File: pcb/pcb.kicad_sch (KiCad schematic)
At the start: 24 parts, among them J1 USB_C_Receptacle_USB2.0_16P, SW1 SW_Push, U1 USBLC6-2SC6, U2 XC6206PxxxMR, U3 STM32F072CBTx

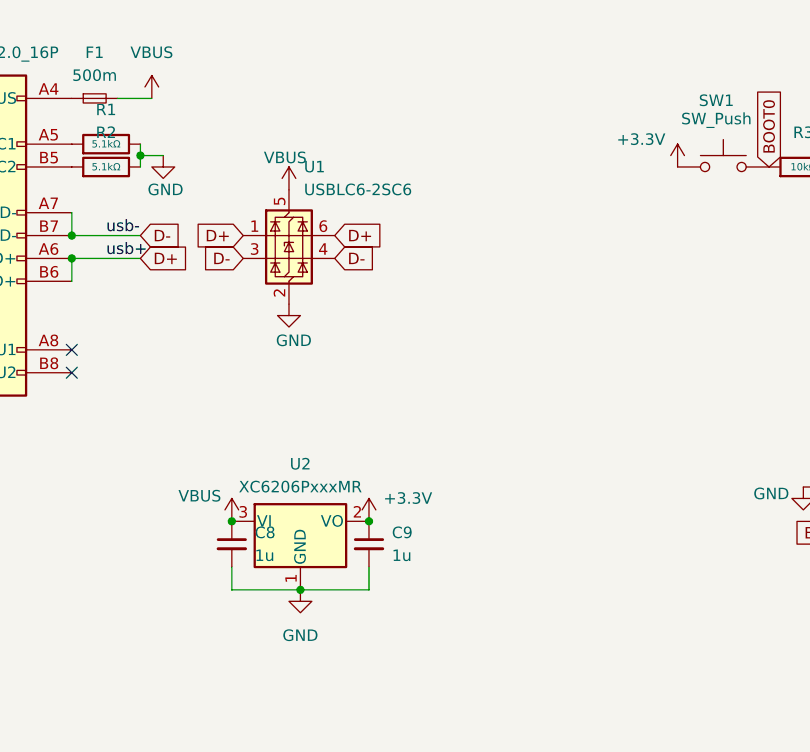
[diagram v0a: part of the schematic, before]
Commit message: Replace some more with LSCPCB library
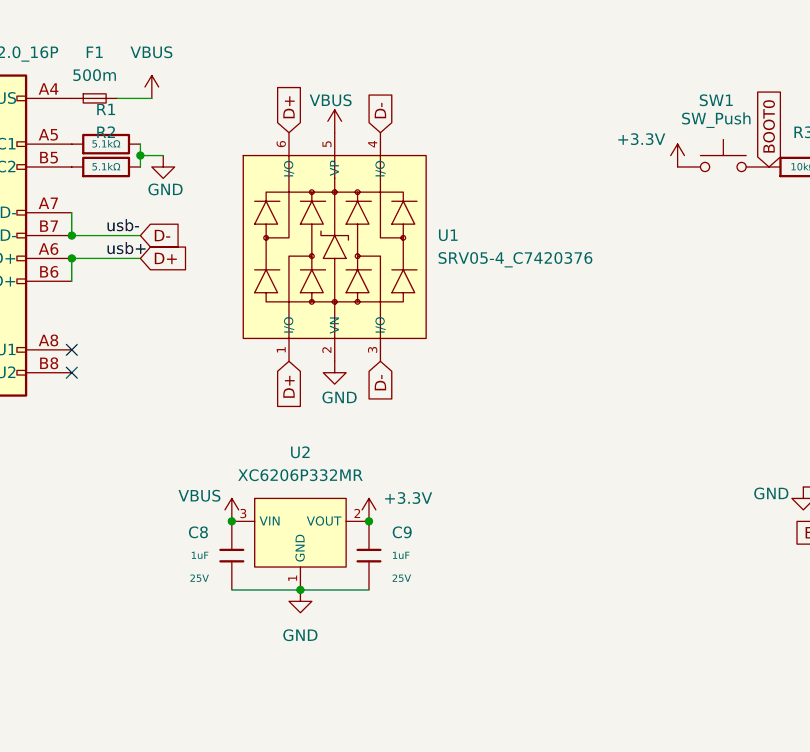
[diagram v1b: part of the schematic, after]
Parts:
- removed C8, C9: 1u, Capacitor_SMD:C_0402_1005Metric, symbol Device:C_Small
- removed U1: USBLC6-2SC6, PCM_marbastlib-various:SOT-23-6-routable, symbol Power_Protection:USBLC6-2SC6
- removed U2: XC6206PxxxMR, Package_TO_SOT_SMD:SOT-23-3, symbol Regulator_Linear:XC6206PxxxMR
- added C8, C9: 1uF, PCM_JLCPCB:C_0402, symbol PCM_JLCPCB-Capacitors:0402,1uF
- added U1: SRV05-4_C7420376, PCM_JLCPCB:SOT-23-6_L2.9-W1.6-P0.95-LS2.8-BL-1, symbol PCM_JLCPCB-Diode-Packages:Package, SRV05-4_C7420376
- added U2: XC6206P332MR, PCM_JLCPCB:SOT-23-3_L2.9-W1.6-P1.90-LS2.8-BR, symbol PCM_JLCPCB-Power:LDO, 3.3V, 0.2A
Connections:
- net +3.3V: now also C9.1, U2.2 (VOUT)
- net D+: now also U1.1 (I/O), U1.6 (I/O)
- net D-: now also U1.3 (I/O), U1.4 (I/O)
- net GND: now also C8.2, C9.2, U1.2 (VN), U2.1 (GND)
- net VBUS: now also C8.1, U1.5 (VP), U2.3 (VIN)

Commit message: matrix connected
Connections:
- net Co10: now also U3.17 (PA7); no longer U3.3 (PC14)
- net Co11: now also U3.16 (PA6); no longer U3.17 (PA7)
- net Co12: now also U3.15 (PA5); no longer U3.10 (PA0)
- net Co13: now also U3.14 (PA4); no longer U3.11 (PA1)
- net Co14: now also U3.13 (PA3); no longer U3.12 (PA2)
- net Co15: now also U3.12 (PA2); no longer U3.13 (PA3)
- net Co5: now also U3.22 (PB11); no longer U3.14 (PA4)
- net Co7: now also U3.20 (PB2); no longer U3.22 (PB11)
- net Co8: now also U3.19 (PB1); no longer U3.15 (PA5)
- net Co9: now also U3.18 (PB0); no longer U3.2 (PC13)
- net Ro2: now also U3.11 (PA1); no longer U3.4 (PC15)
- net Ro3: now also U3.10 (PA0); no longer U3.18 (PB0)
- net Ro4: now also U3.4 (PC15); no longer U3.19 (PB1)
- net Ro5: now also U3.3 (PC14); no longer U3.20 (PB2)
- net Ro6: now also U3.2 (PC13); no longer U3.16 (PA6)
- no-connect marks 2 -> 12

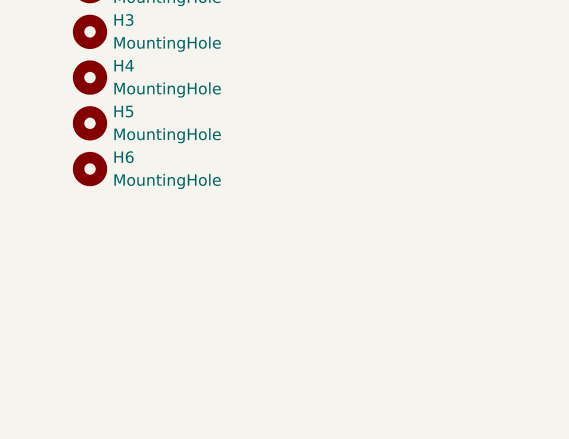
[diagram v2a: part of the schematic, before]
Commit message: fix mouting holes
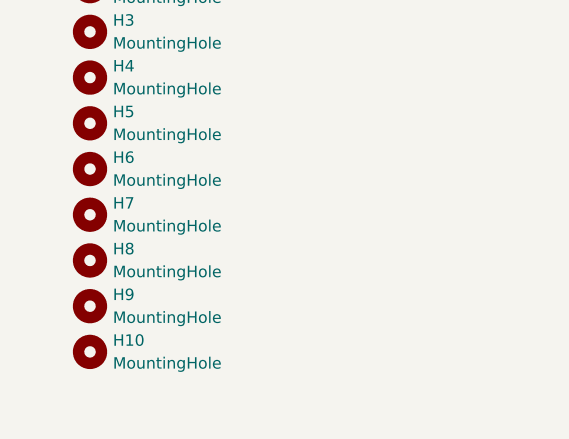
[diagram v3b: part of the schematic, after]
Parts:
- added H10, H7, H8, H9: MountingHole, MountingHole:MountingHole_2mm, symbol Mechanical:MountingHole

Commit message: jlcpcb USB-C
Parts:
- removed J1: USB_C_Receptacle_USB2.0_16P, PCM_marbastlib-various:USB_C_Receptacle_HRO_TYPE-C-31-M-12, symbol Connector:USB_C_Receptacle_USB2.0_16P
- added J1: Connector, USB-TYPE-C-16P, PCM_JLCPCB:TYPE-C-SMD_HX-TYPE-C-16PIN, symbol PCM_JLCPCB-Extended:Connector, USB-TYPE-C-16P
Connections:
- net D+: now also J1.A6 (D+), J1.B6 (D+)
- net D-: now also J1.A7 (D-), J1.B7 (D-)
- net GND: now also J1.A12B1 (GND), J1.B12A1 (GND), J1.S1 (SHIELD)
- net at R1.1: now also J1.A5 (CC1)
- net at R2.1: now also J1.B5 (CC2)
- net at F1.1: now also J1.A9B4 (VBUS), J1.B9A4 (VBUS)
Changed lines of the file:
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@@
 	)
 	(junction
+		(at 57.15 40.64)
+		(diameter 0)
+		(color 0 0 0 0)
+	)
+	(junction
 		(at 232.41 55.88)
 		(diameter 0)
@@
 	)
 	(junction
-		(at 57.15 40.64)
-		(diameter 0)
-		(color 0 0 0 0)
-	)
-	(junction
 		(at 57.15 43.18)
 		(diameter 0)
@@
 		(dnp no)
 		(fields_autoplaced yes)
-		(property "Reference" "#PWR04"
+		(property "Reference" "#PWR05"
 			(at 142.24 39.37 0)
 			(effects
@@
 			(project ""
 				(path "/c1d39311-56a5-4035-b0a7-7ad71eed89a6"
-					(reference "#PWR04")
+					(reference "#PWR05")
 					(unit 1)
 				)
@@
 		(on_board yes)
 		(dnp no)
-		(property "Reference" "#PWR06"
+		(property "Reference" "#PWR07"
 			(at 86.36 60.96 0)
 			(effects
@@
 			(project ""
 				(path "/c1d39311-56a5-4035-b0a7-7ad71eed89a6"
-					(reference "#PWR06")
+					(reference "#PWR07")
 					(unit 1)
 				)
@@
 		(dnp no)
 		(fields_autoplaced yes)
-		(property "Reference" "#PWR07"
+		(property "Reference" "#PWR06"
 			(at 196.85 52.07 0)
 			(effects
@@
 			(project ""
 				(path "/c1d39311-56a5-4035-b0a7-7ad71eed89a6"
-					(reference "#PWR07")
+					(reference "#PWR06")
 					(unit 1)
 				)
@@
 		(on_board yes)
 		(dnp no)
-		(property "Reference" "#PWR05"
+		(property "Reference" "#PWR02"
 			(at 86.36 33.02 0)
 			(effects
@@
 			(project ""
 				(path "/c1d39311-56a5-4035-b0a7-7ad71eed89a6"
-					(reference "#PWR05")
+					(reference "#PWR02")
 					(unit 1)
 				)
@@
 		(on_board yes)
 		(dnp no)
-		(property "Reference" "#PWR03"
+		(property "Reference" "#PWR04"
 			(at 124.46 36.83 0)
 			(effects
@@
 			(project ""
 				(path "/c1d39311-56a5-4035-b0a7-7ad71eed89a6"
-					(reference "#PWR03")
+					(reference "#PWR04")
 					(unit 1)
 				)
@@
 		(on_board yes)
 		(dnp no)
-		(property "Reference" "#PWR02"
+		(property "Reference" "#PWR03"
 			(at 67.31 38.1 0)
 			(effects
@@
 			(project ""
 				(path "/c1d39311-56a5-4035-b0a7-7ad71eed89a6"
-					(reference "#PWR02")
+					(reference "#PWR03")
 					(unit 1)
 				)
@@
 	)
 	(symbol
-		(lib_id "Connector:USB_C_Receptacle_USB2.0_16P")
-		(at 41.91 40.64 0)
-		(unit 1)
-		(exclude_from_sim no)
-		(in_bom yes)
-		(on_board yes)
-		(dnp no)
-		(fields_autoplaced yes)
-		(property "Reference" "J1"
-			(at 41.91 17.78 0)
-			(effects
-				(font
-					(size 1.27 1.27)
-				)
-			)
-		)
-		(property "Value" "USB_C_Receptacle_USB2.0_16P"
-			(at 41.91 20.32 0)
-			(effects
-				(font
-					(size 1.27 1.27)
-				)
-			)
-		)
-		(property "Footprint" "PCM_marbastlib-various:USB_C_Receptacle_HRO_TYPE-C-31-M-12"
-			(at 45.72 40.64 0)
-			(effects
-				(font
-					(size 1.27 1.27)
-				)
-				(hide yes)
-			)
-		)
-		(property "Datasheet" "https://www.usb.org/sites/default/files/documents/usb_type-c.zip"
-			(at 45.72 40.64 0)
-			(effects
-				(font
-					(size 1.27 1.27)
-				)
-				(hide yes)
-			)
-		)
-		(property "Description" "USB 2.0-only 16P Type-C Receptacle connector"
-			(at 41.91 40.64 0)
-			(effects
-				(font
-					(size 1.27 1.27)
-				)
-				(hide yes)
-			)
-		)
-		(pin "A6"
-		)
-		(pin "B7"
-		)
-		(pin "B4"
-		)
-		(pin "B6"
-		)
-		(pin "A5"
-		)
-		(pin "B9"
-		)
-		(pin "A7"
-		)
-		(pin "S1"
-		)
-		(pin "A9"
-		)
-		(pin "B12"
-		)
-		(pin "B1"
-		)
-		(pin "A12"
-		)
-		(pin "A1"
-		)
-		(pin "A4"
-		)
-		(pin "A8"
-		)
-		(pin "B5"
-		)
-		(pin "B8"
-		)
-		(instances
-			(project ""
-				(path "/c1d39311-56a5-4035-b0a7-7ad71eed89a6"
-					(reference "J1")
-					(unit 1)
-				)
-			)
-		)
-	)
-	(symbol
 		(lib_id "PCM_JLCPCB-Capacitors:0402,10uF")
 		(at 241.3 52.07 0)
@@
 					(unit 1)
 				)
+			)
+		)
+	)
+	(symbol
+		(lib_id "PCM_JLCPCB-Extended:Connector, USB-TYPE-C-16P")
+		(at 41.91 40.64 0)
+		(unit 1)
+		(exclude_from_sim no)
+		(in_bom yes)
+		(on_board yes)
+		(dnp no)
+		(fields_autoplaced yes)
+		(property "Reference" "J1"
+			(at 41.91 20.32 0)
+			(effects
+				(font
+					(size 1.27 1.27)
+				)
+			)
+		)
+		(property "Value" "Connector, USB-TYPE-C-16P"
+			(at 44.45 41.91 0)
+			(effects
+				(font
+					(size 1.27 1.27)
+				)
+				(hide yes)
+			)
+		)
+		(property "Footprint" "PCM_JLCPCB:TYPE-C-SMD_HX-TYPE-C-16PIN"
+			(at 41.91 50.8 0)
+			(effects
+				(font
+					(size 1.27 1.27)
+					(italic yes)
+				)
+				(hide yes)
+			)
+		)
+		(property "Datasheet" "https://atta.szlcsc.com/upload/public/pdf/source/20220920/0EF8F885FCCEA71F60E9E85152155021.pdf"
+			(at 39.624 40.513 0)
+			(effects
+				(font
+					(size 1.27 1.27)
+				)
+				(justify left)
+				(hide yes)
+			)
+		)
+		(property "Description" "3A 1 Horizontal attachment 16P Female -25℃~+85℃ Type-C SMD USB Connectors ROHS"
+			(at 44.45 39.37 0)
+			(effects
+				(font
+					(size 1.27 1.27)
+				)
+				(hide yes)
+			)
+		)
+		(property "LCSC" "C2927039"
+			(at 44.45 39.37 0)
+			(effects
+				(font
+					(size 1.27 1.27)
+				)
+				(hide yes)
+			)
+		)
+		(pin "B8"
+		)
+		(pin "A8"
+		)
+		(pin "A7"
+		)
+		(pin "B6"
+		)
+		(pin "A6"
+		)
+		(pin "B7"
+		)
+		(pin "S1"
+		)
+		(pin "B9A4"
+		)
+		(pin "A12B1"
+		)
+		(pin "B5"
+		)
+		(pin "B12A1"
+		)
+		(pin "A5"
+		)
+		(pin "A9B4"
+		)
+		(instances
+			(project ""
+				(path "/c1d39311-56a5-4035-b0a7-7ad71eed89a6"
+					(reference "J1")
+					(unit 1)
+				)

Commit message: Before production
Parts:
- renumbered J1 to U1, U1 to U2, U2 to U3, U3 to U4
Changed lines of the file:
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@@
 		(dnp no)
 		(fields_autoplaced yes)
-		(property "Reference" "U3"
+		(property "Reference" "U4"
 			(at 168.5133 142.24 0)
 			(effects
@@
 			(project ""
 				(path "/c1d39311-56a5-4035-b0a7-7ad71eed89a6"
-					(reference "U3")
+					(reference "U4")
 					(unit 1)
 				)
@@
 		(dnp no)
 		(fields_autoplaced yes)
-		(property "Reference" "U2"
+		(property "Reference" "U3"
 			(at 82.55 64.77 0)
 			(effects
@@
 			(project ""
 				(path "/c1d39311-56a5-4035-b0a7-7ad71eed89a6"
-					(reference "U2")
+					(reference "U3")
 					(unit 1)
 				)
@@
 		(dnp no)
 		(fields_autoplaced yes)
-		(property "Reference" "U1"
+		(property "Reference" "U2"
 			(at 97.79 40.6399 0)
 			(effects
@@
 			(project ""
 				(path "/c1d39311-56a5-4035-b0a7-7ad71eed89a6"
-					(reference "U1")
+					(reference "U2")
 					(unit 1)
 				)
@@
 		(dnp no)
 		(fields_autoplaced yes)
-		(property "Reference" "J1"
+		(property "Reference" "U1"
 			(at 41.91 20.32 0)
 			(effects
@@
 			(project ""
 				(path "/c1d39311-56a5-4035-b0a7-7ad71eed89a6"
-					(reference "J1")
+					(reference "U1")
 					(unit 1)
 				)
